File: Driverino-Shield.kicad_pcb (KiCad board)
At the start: 2 copper layers, 68.6 x 53.3 mm, 57 parts, among them P1 Power, P10 MOT, P11 HALL, P2 Analog, P3 Digital, P4 Digital, P5 CONN_01X01, P6 CONN_01X01, P7 CONN_01X01, P8 CONN_01X01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

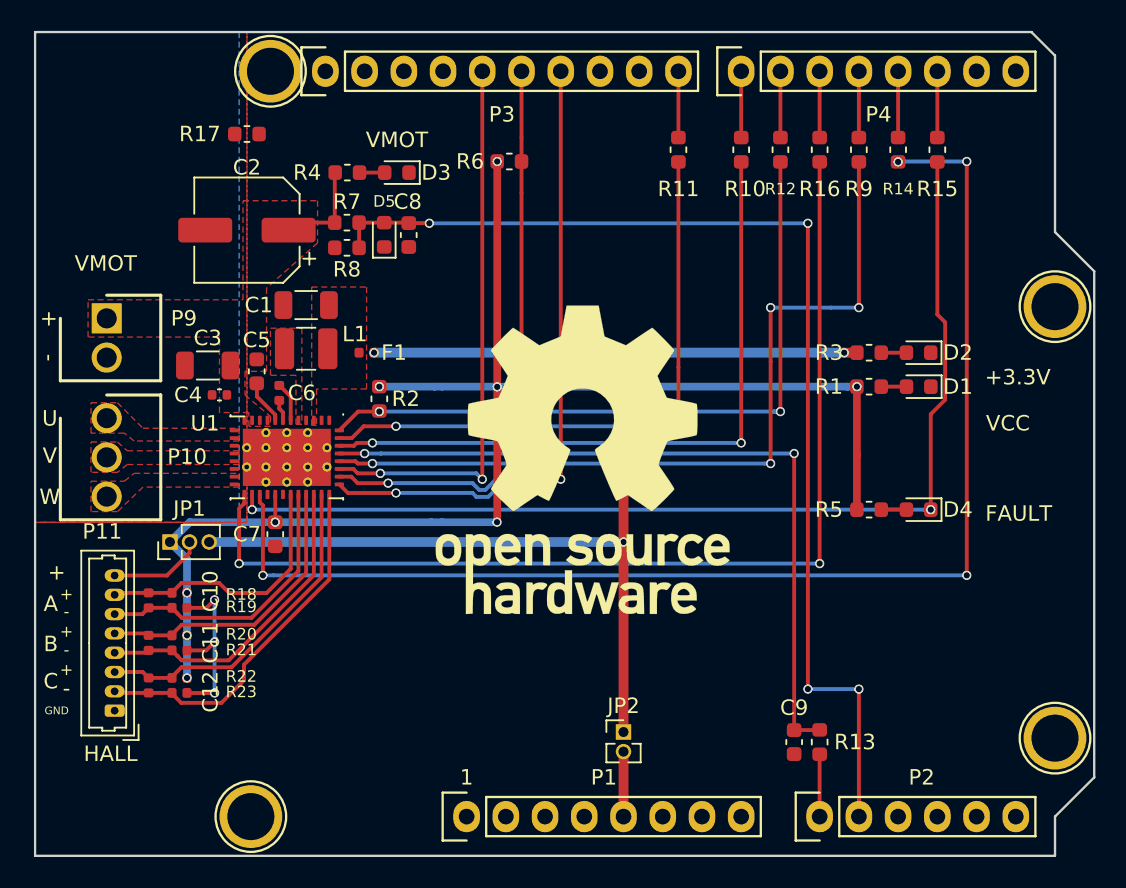
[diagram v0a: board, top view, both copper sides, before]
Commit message: Add kitspace.yaml, rename gerber folder
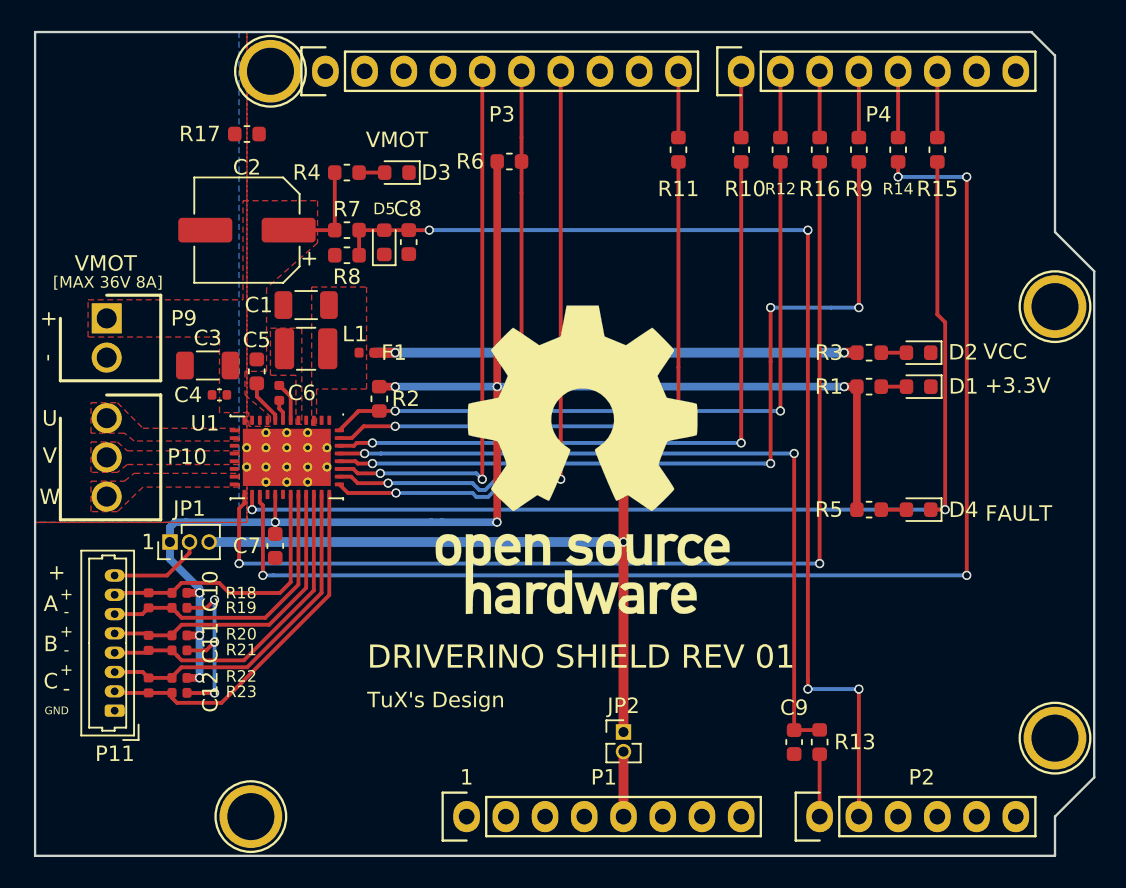
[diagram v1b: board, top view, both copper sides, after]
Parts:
- moved C7 0.76 mm to (126.5, 106.3)
- moved R7 0.49 mm to (131.2, 85.9)
- moved D5 0.49 mm to (133.6, 86.6)
- moved R8 0.48 mm to (131.2, 87.5)
- moved C8 0.46 mm to (135.2, 86.6)
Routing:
- net +3.3V: track 95.0 -> 99.1 mm, vias 9 -> 8
- net /FAULT: track 68.2 -> 69.7 mm
- net VCC: track 82.7 -> 84.0 mm
- net +36V: track 6.44 -> 7.44 mm
- net /FGOUT: track 45.5 -> 46.5 mm
- net /HCP: track 21.7 -> 22.3 mm
- net /HBN: track 20.8 -> 21.3 mm
- net /HBP: track 19.3 -> 19.8 mm
- net /HAN: track 18.6 -> 19.1 mm
- net /HAP: track 17.5 -> 18.0 mm
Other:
- board text added: "DRIVERINO SHIELD REV 01"
- board text added: "TuX's Design"
- board text added: "[MAX 36V 8A]"
- board text removed: "HALL"

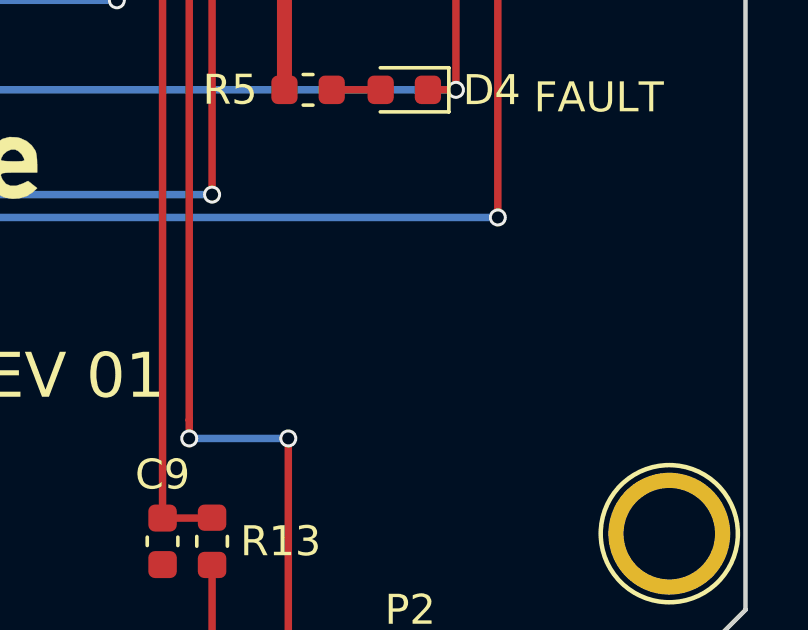
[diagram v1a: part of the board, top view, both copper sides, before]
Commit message: .gitignore update, made-with-kicad logo
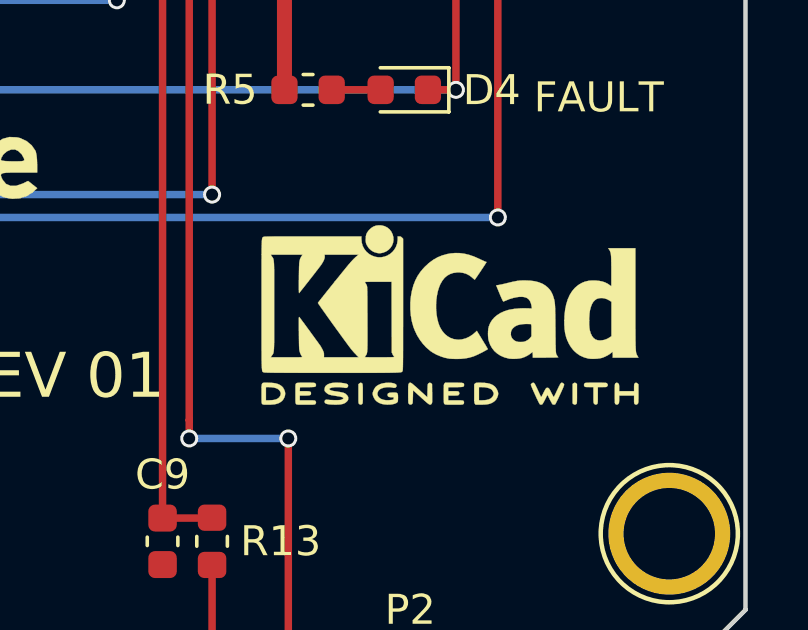
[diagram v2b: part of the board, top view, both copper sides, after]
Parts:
- added REF**: KiCad-Logo2_5mm_SilkScreen, Symbol:KiCad-Logo2_5mm_SilkScreen, F.Cu at (169.7, 111.4)

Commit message: Changed F1 footprint, BOM update
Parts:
- F1: footprint Fuse:Fuse_0402_1005Metric -> Fuse:Fuse_1206_3216Metric_Castellated
- moved F1 1.04 mm to (133.5, 93.8)
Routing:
- net VCC: track 84.0 -> 80.7 mm
